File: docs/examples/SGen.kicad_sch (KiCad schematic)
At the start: 23 parts, among them Q1 2N3904, Q2 2N3904

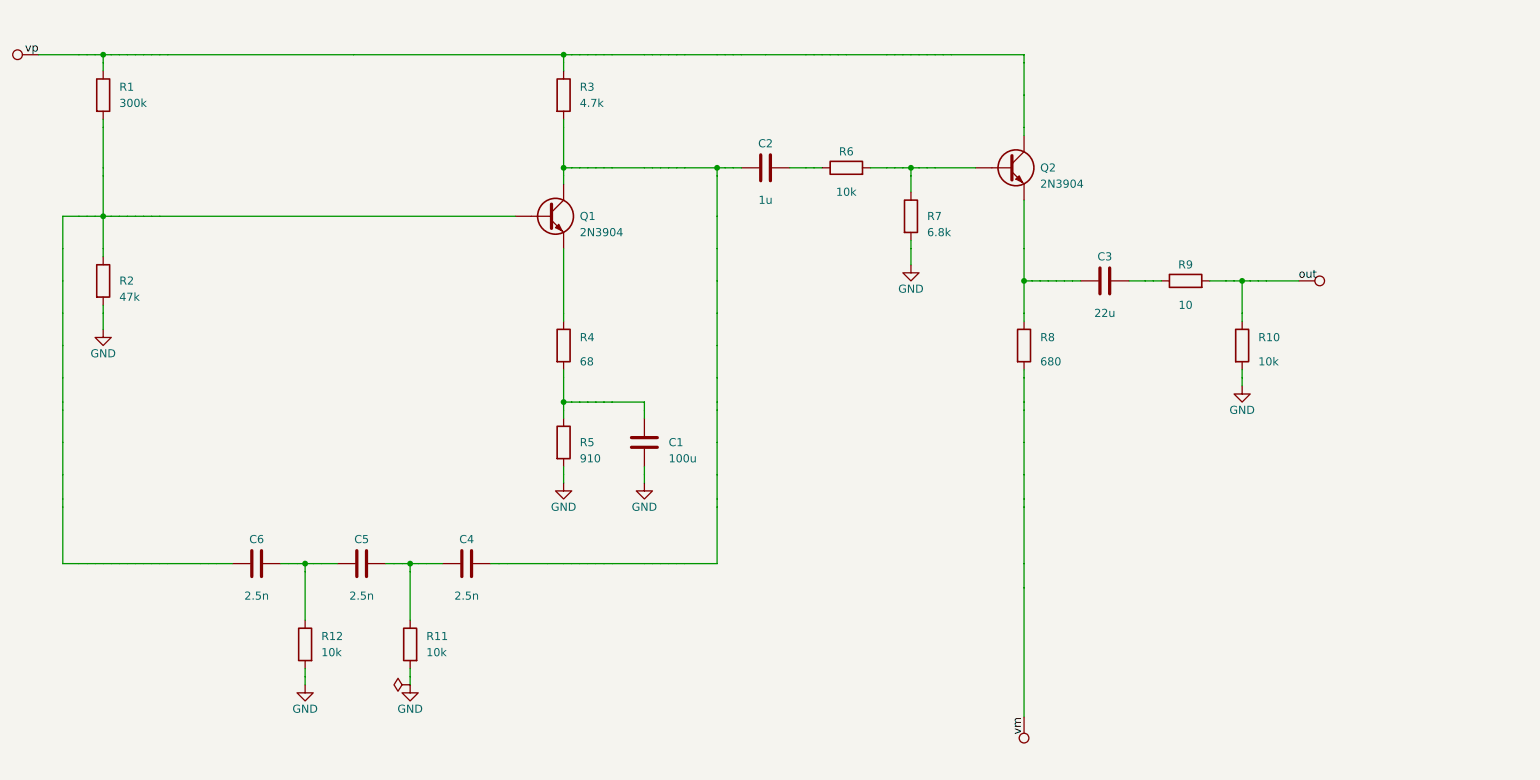
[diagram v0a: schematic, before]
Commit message: Power-net labels drawn as power symbols (registry), axis-flip tie-break (mirror before 180 deg), rotated()/mirrored() API, readable mirror y in JSON; sgen uses <GND> and PS<in> with no explicit orientation
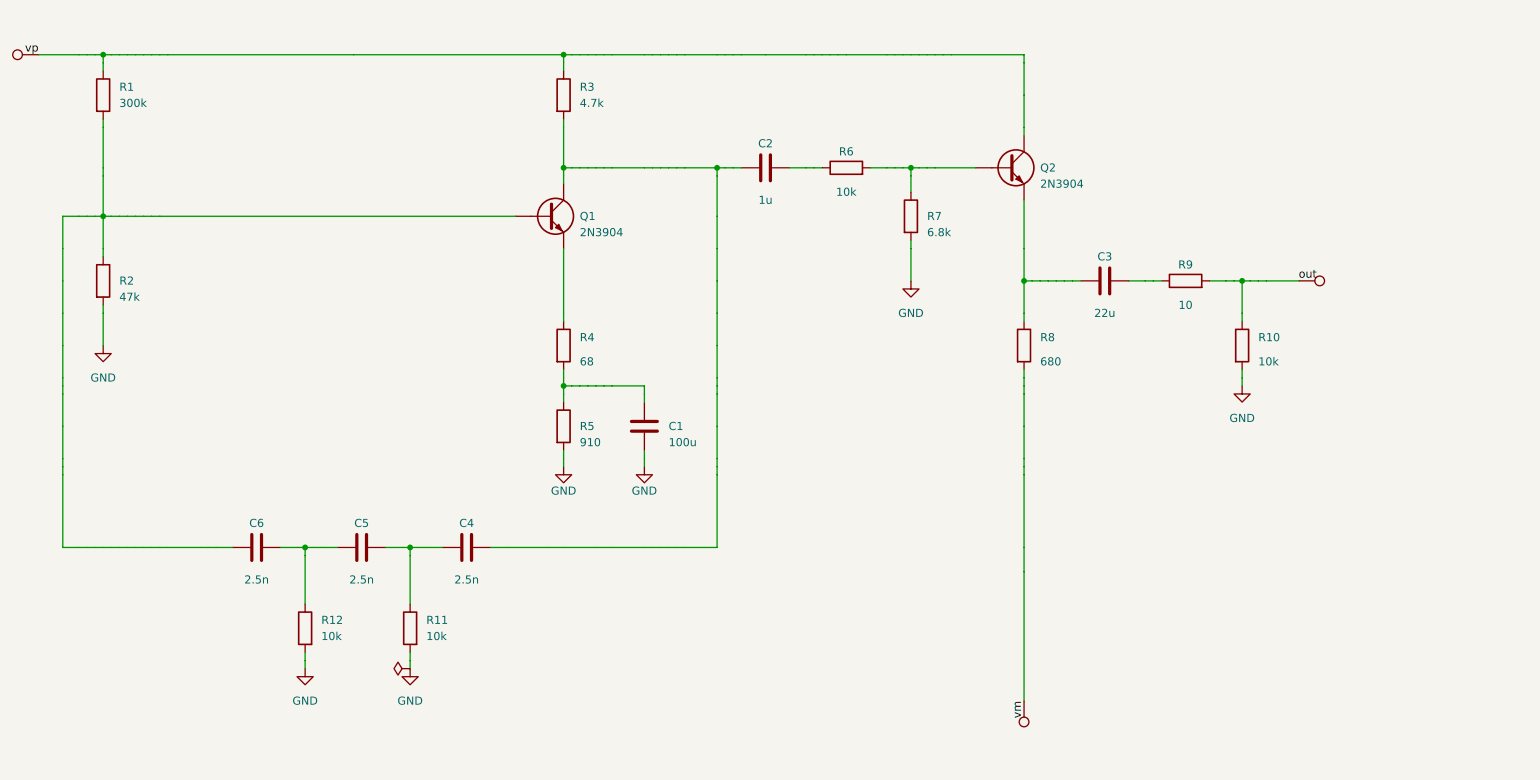
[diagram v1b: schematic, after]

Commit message: sgen: hierarchical composition (PHASE_SHIFT in OSCILLATOR, OUTPUT_AMP from CK on, 5-line SGEN top level); skill: hierarchical design and port-side interface guidance
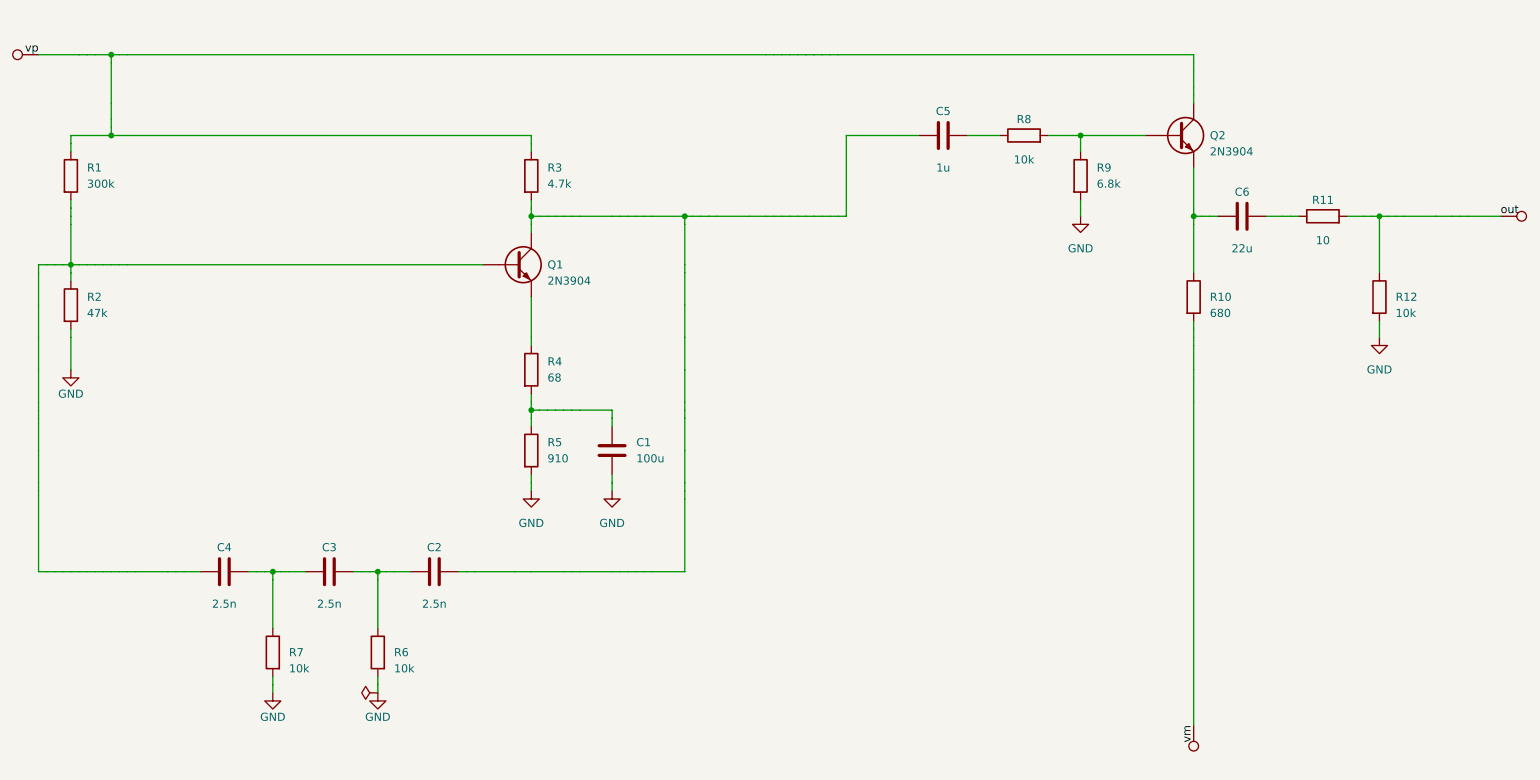
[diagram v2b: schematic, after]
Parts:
- C1: yasdl_path CE -> OSC.CE
- C2: value 1u -> 2.5n; yasdl_path CK -> OSC.PS.C1
- C3: value 22u -> 2.5n; yasdl_path COUT -> OSC.PS.C2
- C4: yasdl_path PS.C1 -> OSC.PS.C3
- C5: value 2.5n -> 1u; yasdl_path PS.C2 -> AMP.CK
- C6: value 2.5n -> 22u; yasdl_path PS.C3 -> AMP.COUT
- Q1: yasdl_path Q1 -> OSC.Q1
- Q2: yasdl_path Q2 -> AMP.Q2
- R1: yasdl_path RA -> OSC.RA
- R10: value 10k -> 680; yasdl_path RBLD -> AMP.RE2
- R11: value 10k -> 10; yasdl_path PS.R1 -> AMP.ROUT
- R12: yasdl_path PS.R2 -> AMP.RBLD
- R2: yasdl_path RB -> OSC.RB
- R3: yasdl_path RC -> OSC.RC
- R4: yasdl_path REUP -> OSC.REUP
- R5: yasdl_path REDN -> OSC.REDN
- R6: yasdl_path RBUF -> OSC.PS.R1
- R7: value 6.8k -> 10k; yasdl_path RBIN -> OSC.PS.R2
- R8: value 680 -> 10k; yasdl_path RE2 -> AMP.RBUF
- R9: value 10 -> 6.8k; yasdl_path ROUT -> AMP.RBIN
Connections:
- net GND: now also R6.2, R9.2; no longer R10.2, R11.2
- net out: now also R11.2, R12.1; no longer R10.1, R9.2
- net vm: now also R10.2; no longer R8.2
- net at C2.1, Q1.C, R3.2: now also C5.1; no longer C4.1
- net at Q1.B, R1.2, R2.1: now also C4.2; no longer C6.2
- net at C2.2, R6.1: now also C3.1
- net at C3.2: now also C4.1, R7.1; no longer R9.1
- new net: C6.2, R11.1
- new net: C6.1, Q2.E, R10.1
- new net: C5.2, R8.1
- new net: Q2.B, R8.2, R9.1

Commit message: sgen: {vp} on top of SGEN (power); task pin order via port_order=SGEN_PINS; skill/README note
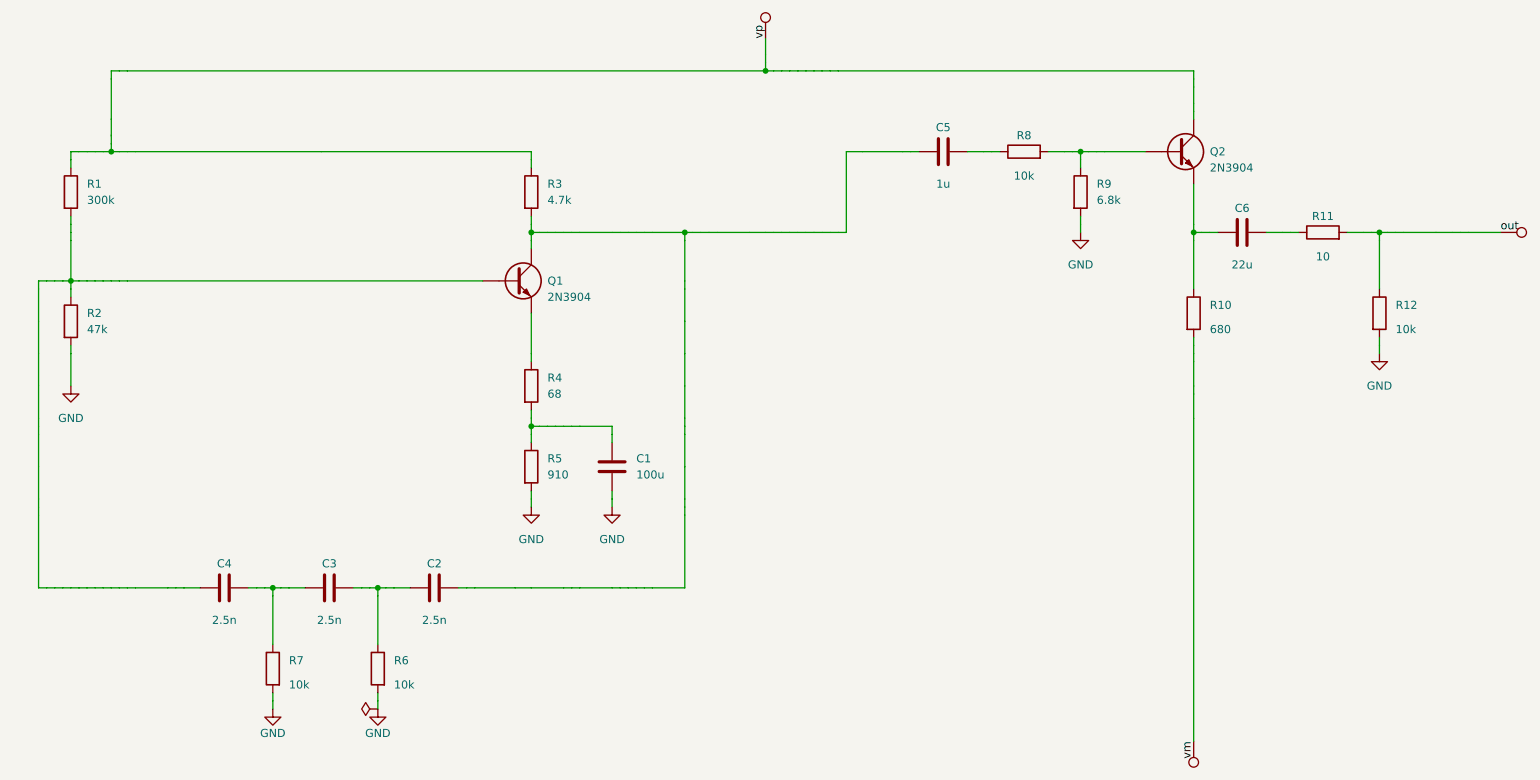
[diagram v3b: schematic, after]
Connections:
- net out: now also TP2.1; no longer TP1.1
- net vm: now also TP3.1; no longer TP2.1
- net vp: now also TP1.1; no longer TP3.1
